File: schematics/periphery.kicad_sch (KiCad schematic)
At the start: 27 parts, among them J11 WF-2, J12 WF-2, J13 WF-2, Q501 2N7002, Q502 2N7002, Q503 2N7002

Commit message: Множественные обновления схем
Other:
- company: Филимонов и К -> (none)
- title: (none) -> OctopusNode
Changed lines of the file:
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@@
 	(paper "A4")
 	(title_block
-		(company "Филимонов и К")
+		(title "OctopusNode")
 		(comment 2 "Филимонов С.В.")
 		(comment 3 "Семеренко Д.А.")

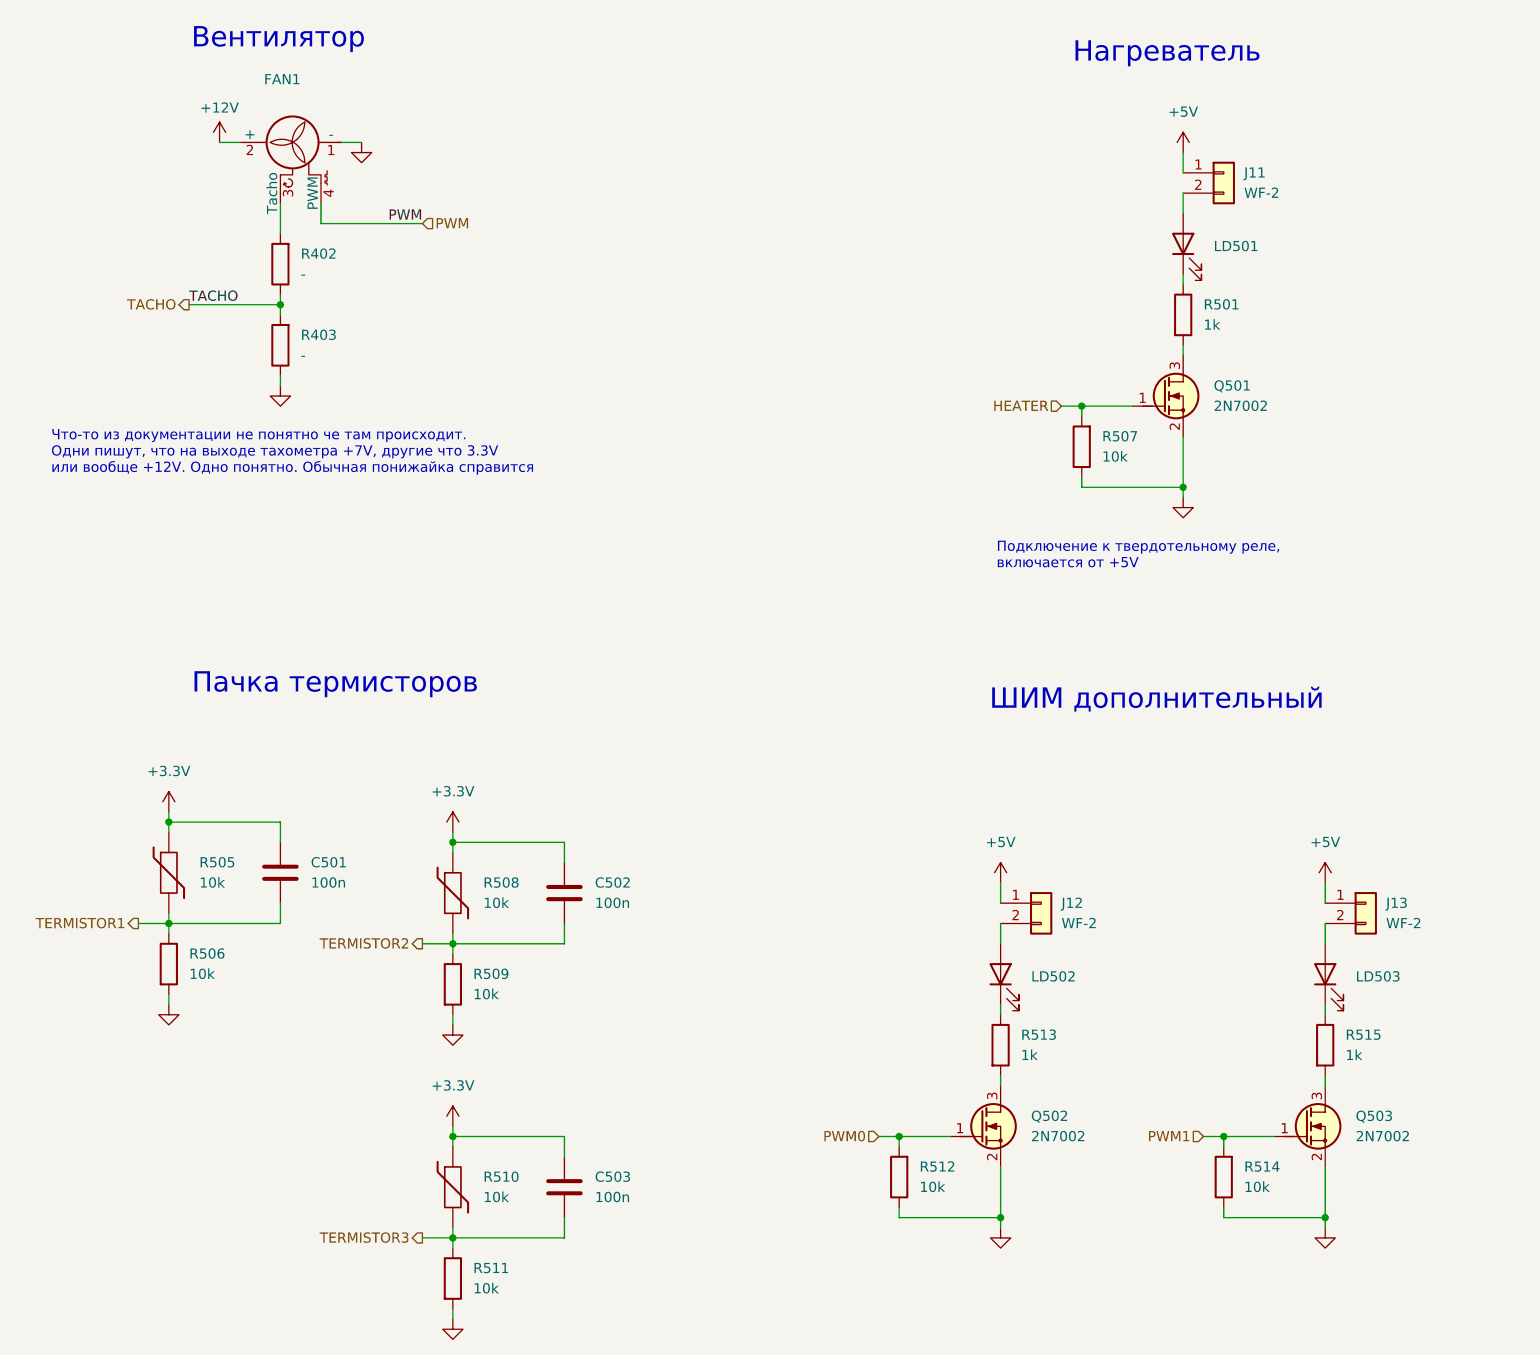
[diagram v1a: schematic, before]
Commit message: Обновил обозначения, а то старая нумерация была специфической
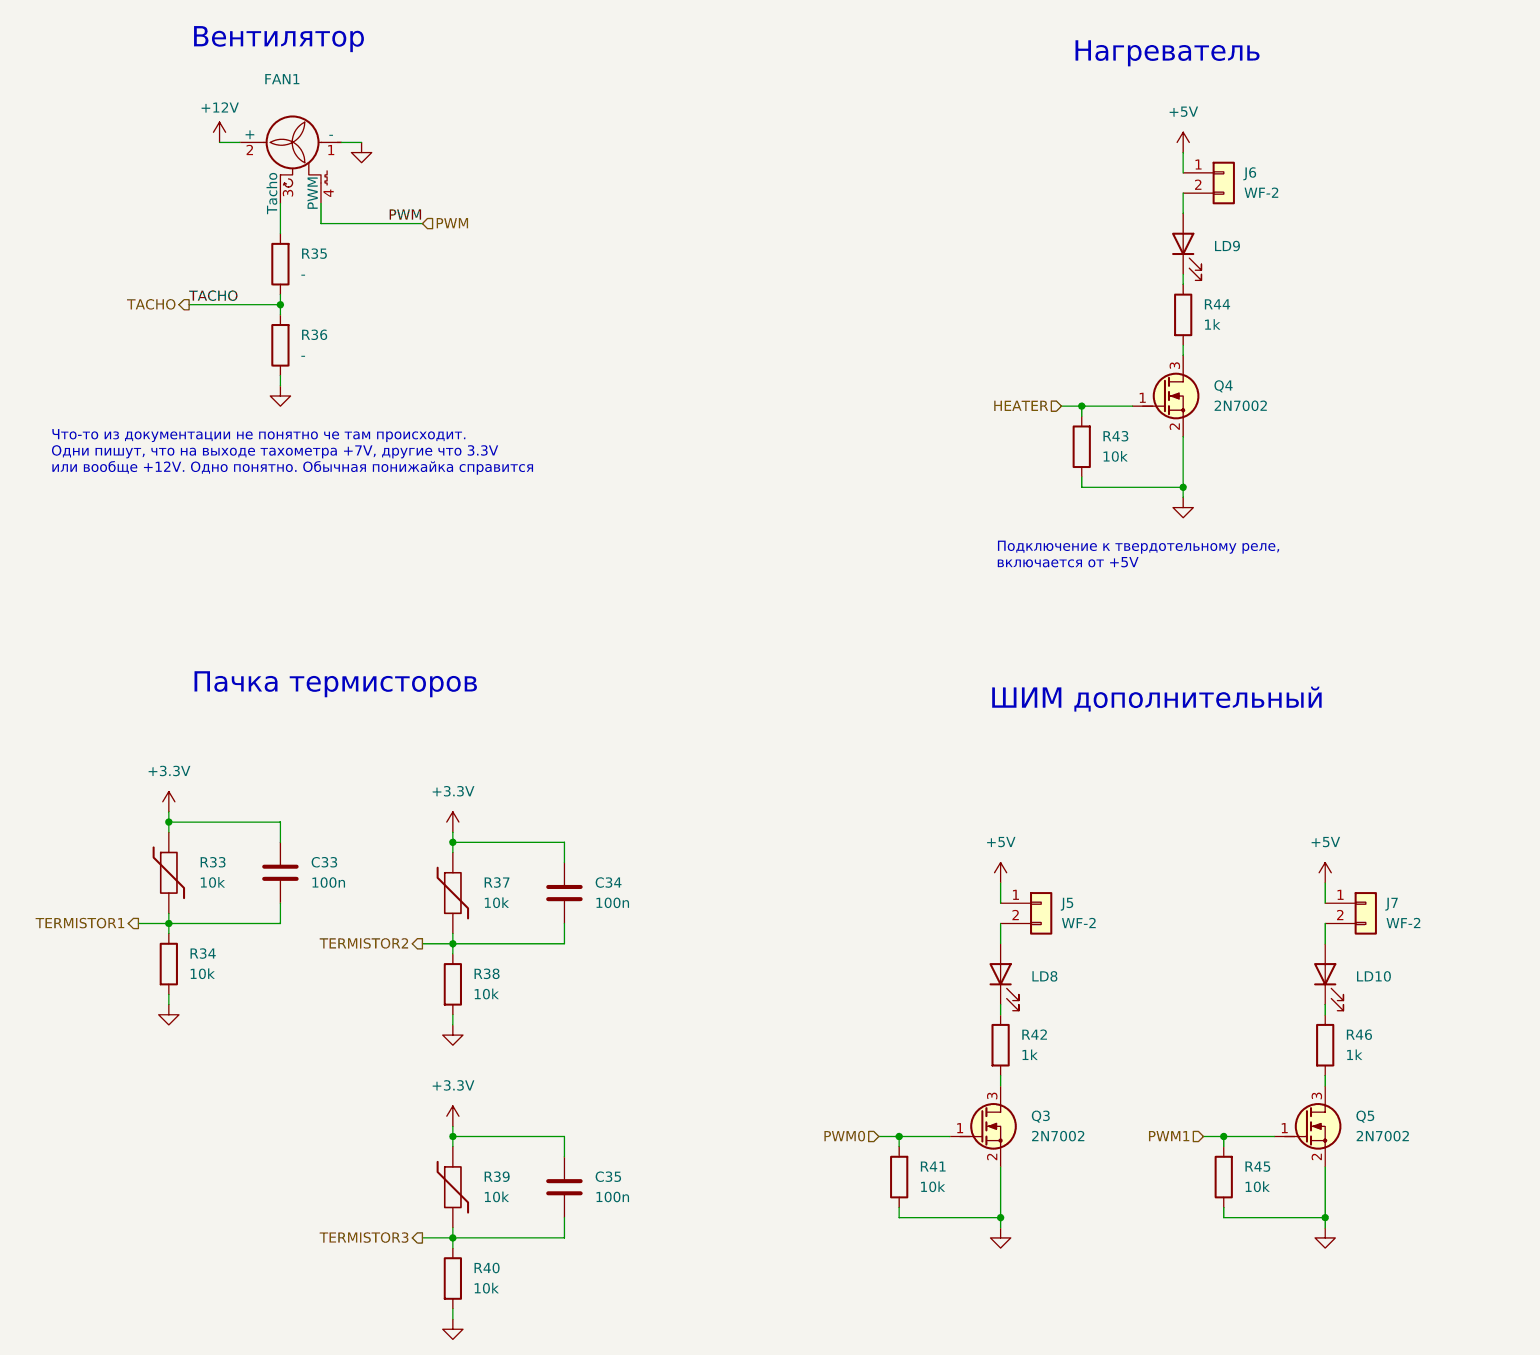
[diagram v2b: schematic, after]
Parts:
- renumbered C501 to C33, C502 to C34, C503 to C35, J12 to J5, J11 to J6, J13 to J7, LD503 to LD10, LD502 to LD8, LD501 to LD9, Q502 to Q3, Q501 to Q4, Q503 to Q5, R505 to R33, R506 to R34, R402 to R35, R403 to R36, R508 to R37, R509 to R38, R510 to R39, R511 to R40, R512 to R41, R513 to R42, R507 to R43, R501 to R44, R514 to R45, R515 to R46
